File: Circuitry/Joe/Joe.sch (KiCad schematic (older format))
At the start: 41 parts

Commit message: fixed up joe
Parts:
- removed Q? (x4): 2N7000, Package_TO_SOT_THT:TO-92_Inline, symbol Transistor_FET:2N7000
- removed R? (x8): 10k, symbol Device:R
- added BT?: Battery_Cell, symbol Device:Battery_Cell
- added J?: USB_B_Micro, symbol Connector:USB_B_Micro
- added U?: AP2127N-3.3, Package_TO_SOT_SMD:SOT-23, symbol Regulator_Linear:AP2127N-3.3
- R? (x4): value R -> 1k
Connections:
- net labels added: CRYSTAL, D+, D-, RCLK, SER, SRCLK, VBUS, ~SRCLR
- net labels removed: CRY, CRYSTAL2, DATA, E0, E1, E2, MOSO, SCL2, SDA2, SQW2, S_CLR
- wire segments 125 -> 101
- no-connect marks 4 -> 15
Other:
- note removed: "Level Shifters"

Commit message: Joe: RTC changed to soic8, added labels to screw terminal, removed shift regs Burt: added shift reg
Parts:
- removed U?: DS3231M, Package_SO:SOIC-16W_7.5x10.3mm_P1.27mm, symbol Timer_RTC:DS3231M
- removed U?: 74HC595, symbol 74xx:74HC595
- added U?: DS3231MZ, Package_SO:SOIC-8_3.9x4.9mm_P1.27mm, symbol Timer_RTC:DS3231MZ
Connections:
- net labels removed: BL1, BL2, BL3, BL4, BL5, BL6, BL7, BL8, BWL
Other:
- note added: "Burn Wire Output 1 for Pyrolysis"
- note added: "Burn Wire Output 2 for Pyrolysis"
- note added: "Img Sensor Data Input"
- note added: "RX Output for Img Processor"
- note added: "TX Output for Img Processor"
- note added: "Temp Sensor Data Input"
- note removed: "Shift Register (for launcher bw)"
- moved on the sheet: U?
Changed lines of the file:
@@
 	2450 1450 2975 1450
-$Comp
-L Timer_RTC:DS3231M U?
-U 1 1 5D1CA19F
-P 1950 1650
-F 0 "U?" H 1150 2575 50  0000 C CNN
-F 1 "DS3231M" H 900 2575 50  0000 C CNN
-F 2 "Package_SO:SOIC-16W_7.5x10.3mm_P1.27mm" H 1950 1050 50  0001 C CNN
-F 3 "http://datasheets.maximintegrated.com/en/ds/DS3231.pdf" H 2220 1700 50  0001 C CNN
-	1    1950 1650
-	1    0    0    -1
-$EndComp
 $Comp
 L Device:R R?
@@
 Text Label 10875 3150 0    50   ~ 0
 PHO4
-Text Label 6850 4600 2    50   ~ 0
+Text Label 4550 2875 2    50   ~ 0
 TEMP
 Wire Wire Line
@@
 Wire Wire Line
 	10650 2450 10850 2450
-Text Label 6850 4700 2    50   ~ 0
+Text Label 4550 2975 2    50   ~ 0
 CVBS
-$Comp
-L Joe-rescue:UFDFPN8-MC-Custom U?
-U 1 1 5D2D63AB
-P 4925 6900
-F 0 "U?" H 4950 7265 50  0000 C CNN
-F 1 "UFDFPN8-MC" H 4950 7174 50  0000 C CNN
-F 2 "" H 4925 6900 50  0001 C CNN
-F 3 "https://www.st.com/content/ccc/resource/technical/document/datasheet/80/4e/8c/54/f2/63/4c/4a/CD00001012.pdf/files/CD00001012.pdf/jcr:content/translations/en.CD00001012.pdf" H 4925 6900 50  0001 C CNN
-	1    4925 6900
-	1    0    0    -1
-$EndComp
-Wire Wire Line
-	5275 6800 5475 6800
-Text Label 5275 6900 0    50   ~ 0
+Wire Wire Line
+	3725 6025 3925 6025
+Text Label 3725 6125 0    50   ~ 0
 WC
-Text Label 5275 7000 0    50   ~ 0
+Text Label 3725 6225 0    50   ~ 0
 SCL
-Text Label 5275 7100 0    50   ~ 0
+Text Label 3725 6325 0    50   ~ 0
 SDA
 $Comp
 L power:GND #PWR?
 U 1 1 5D2C2E70
-P 4450 7100
-F 0 "#PWR?" H 4450 6850 50  0001 C CNN
-F 1 "GND" H 4455 6927 50  0000 C CNN
-F 2 "" H 4450 7100 50  0001 C CNN
-F 3 "" H 4450 7100 50  0001 C CNN
-	1    4450 7100
-	1    0    0    -1
-$EndComp
-Wire Wire Line
-	4625 7100 4450 7100
+P 2900 6325
+F 0 "#PWR?" H 2900 6075 50  0001 C CNN
+F 1 "GND" H 2905 6152 50  0000 C CNN
+F 2 "" H 2900 6325 50  0001 C CNN
+F 3 "" H 2900 6325 50  0001 C CNN
+	1    2900 6325
+	1    0    0    -1
+$EndComp
+Wire Wire Line
+	3075 6325 2900 6325
 Text Label 10875 4250 0    50   ~ 0
 WC
@@
 Wire Notes Line
 	2650 3825 2650 2475
-Text Notes 4325 6350 0    50   ~ 0
-EEPROM\n
-$Comp
-L 74xx:74HC595 U?
-U 1 1 5D4B08F4
-P 3525 6575
-F 0 "U?" H 2750 7550 50  0000 C CNN
-F 1 "74HC595" H 2875 7450 50  0000 C CNN
-F 2 "" H 3525 6575 50  0001 C CNN
-F 3 "http://www.ti.com/lit/ds/symlink/sn74hc595.pdf" H 3525 6575 50  0001 C CNN
-	1    3525 6575
-	1    0    0    -1
-$EndComp
-Text Notes 6775 4425 0    50   ~ 0
+Text Notes 4475 2700 0    50   ~ 0
 Joe <--> Burt\n
-$Comp
-L power:GND #PWR?
-U 1 1 5D4CD56F
-P 3525 7275
-F 0 "#PWR?" H 3525 7025 50  0001 C CNN
-F 1 "GND" H 3530 7102 50  0000 C CNN
-F 2 "" H 3525 7275 50  0001 C CNN
-F 3 "" H 3525 7275 50  0001 C CNN
-	1    3525 7275
-	1    0    0    -1
-$EndComp
 Text Label 10875 4350 0    50   ~ 0
 SER
-Text Label 3125 6175 2    50   ~ 0
-SER
-Text Label 3925 6175 0    50   ~ 0
-BL1
-Text Label 3925 6275 0    50   ~ 0
-BL2
-Text Label 3925 6375 0    50   ~ 0
-BL3
-Text Label 3925 6475 0    50   ~ 0
-BL4
-Text Label 3925 6575 0    50   ~ 0
-BL5
-Text Label 3925 6675 0    50   ~ 0
-BL6
-Text Label 3925 6775 0    50   ~ 0
-BL7
-Text Label 3925 6875 0    50   ~ 0
-BL8
-Text Label 3125 6775 2    50   ~ 0
-OE
 Text Label 10875 4450 0    50   ~ 0
 OE
@@
 Text Label 10850 2150 0    50   ~ 0
 BP2
-Text Label 3125 6475 2    50   ~ 0
-~SRCLR
 Wire Notes Line
 	2650 3875 4150 3875
@@
 Wire Notes Line
 	2650 3875 2650 5375
-Wire Notes Line
-	2650 5425 4150 5425
-Wire Notes Line
-	4150 5425 4150 7750
-Wire Notes Line
-	4150 7750 2650 7750
-Wire Notes Line
-	2650 7750 2650 5425
-Text Notes 2700 5550 0    50   ~ 0
-Shift Register (for launcher bw)
 $Comp
 L Joe-rescue:DF12-20DS-Custom U?
@@
 Wire Notes Line
 	6200 500  4050 500
-Text Label 6850 5200 2    50   ~ 0
-BWL
-Text Label 6850 5000 2    50   ~ 0
+Text Label 4550 3275 2    50   ~ 0
 BP1
-Text Label 6850 5100 2    50   ~ 0
+Text Label 4550 3375 2    50   ~ 0
 BP2
 $Comp
@@
 Wire Wire Line
 	10650 2550 10875 2550
-Text Label 3125 6375 2    50   ~ 0
-SRCLK
-Text Label 3125 6675 2    50   ~ 0
-RCLK
-Wire Wire Line
-	4625 7000 4450 7000
-Wire Wire Line
-	4450 7000 4450 7100
-Connection ~ 4450 7100
-Wire Wire Line
-	4625 6900 4450 6900
-Wire Wire Line
-	4450 6900 4450 7000
-Connection ~ 4450 7000
-Wire Wire Line
-	4625 6800 4450 6800
-Wire Wire Line
-	4450 6800 4450 6900
-Connection ~ 4450 6900
+Wire Wire Line
+	3075 6225 2900 6225
+Wire Wire Line
+	2900 6225 2900 6325
+Connection ~ 2900 6325
+Wire Wire Line
+	3075 6125 2900 6125
+Wire Wire Line
+	2900 6125 2900 6225
+Connection ~ 2900 6225
+Wire Wire Line
+	3075 6025 2900 6025
+Wire Wire Line
+	2900 6025 2900 6125
+Connection ~ 2900 6125
 $Comp
 L power:+3V3 #PWR?
 U 1 1 5D3707C8
-P 5475 6800
-F 0 "#PWR?" H 5475 6650 50  0001 C CNN
-F 1 "+3V3" H 5490 6973 50  0000 C CNN
-F 2 "" H 5475 6800 50  0001 C CNN
-F 3 "" H 5475 6800 50  0001 C CNN
-	1    5475 6800
-	1    0    0    -1
-$EndComp
-$Comp
-L power:+3V3 #PWR?
-U 1 1 5D371FC8
-P 3525 5975
-F 0 "#PWR?" H 3525 5825 50  0001 C CNN
-F 1 "+3V3" H 3540 6148 50  0000 C CNN
-F 2 "" H 3525 5975 50  0001 C CNN
-F 3 "" H 3525 5975 50  0001 C CNN
-	1    3525 5975
+P 3925 6025
+F 0 "#PWR?" H 3925 5875 50  0001 C CNN
+F 1 "+3V3" H 3940 6198 50  0000 C CNN
+F 2 "" H 3925 6025 50  0001 C CNN
+F 3 "" H 3925 6025 50  0001 C CNN
+	1    3925 6025
 	1    0    0    -1
 $EndComp
@@
 Text Label 10875 3950 0    50   ~ 0
 ~SRCLR
+Text Notes 2775 5575 0    50   ~ 0
+EEPROM\n
+$Comp
+L Joe-rescue:UFDFPN8-MC-Custom U?
+U 1 1 5D2D63AB
+P 3375 6125
+F 0 "U?" H 3400 6490 50  0000 C CNN
+F 1 "UFDFPN8-MC" H 3400 6399 50  0000 C CNN
+F 2 "" H 3375 6125 50  0001 C CNN
+F 3 "https://www.st.com/content/ccc/resource/technical/document/datasheet/80/4e/8c/54/f2/63/4c/4a/CD00001012.pdf/files/CD00001012.pdf/jcr:content/translations/en.CD00001012.pdf" H 3375 6125 50  0001 C CNN
+	1    3375 6125
+	1    0    0    -1
+$EndComp
+Text Label 4550 3075 2    50   ~ 0
+TX
+Text Label 4550 3175 2    50   ~ 0
+RX
+Text Label 4550 3475 2    50   ~ 0
+SER
+Text Label 4550 3575 2    50   ~ 0
+SRCLK
+Text Label 4550 3675 2    50   ~ 0
+RCLK
+$Comp
+L Timer_RTC:DS3231MZ U?
+U 1 1 5D2C648B
+P 1950 1650
+F 0 "U?" H 1950 1161 50  0000 C CNN
+F 1 "DS3231MZ" H 1950 1070 50  0000 C CNN
+F 2 "Package_SO:SOIC-8_3.9x4.9mm_P1.27mm" H 1950 1150 50  0001 C CNN
+F 3 "http://datasheets.maximintegrated.com/en/ds/DS3231M.pdf" H 1950 1050 50  0001 C CNN
+	1    1950 1650
+	1    0    0    -1
+$EndComp
+Text Notes 5325 2875 0    39   ~ 0
+Temp Sensor Data Input
+Text Notes 5325 2975 0    39   ~ 0
+Img Sensor Data Input
+Text Notes 5325 3075 0    39   ~ 0
+TX Output for Img Processor
+Text Notes 5325 3175 0    39   ~ 0
+RX Output for Img Processor
+Text Notes 5325 3275 0    39   ~ 0
+Burn Wire Output 1 for Pyrolysis
+Text Notes 5325 3375 0    39   ~ 0
+Burn Wire Output 2 for Pyrolysis
 $EndSCHEMATC

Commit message: complete screw terminal, labeling, etc. done for FINAL REVIEW
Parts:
- added J?: Screw_Terminal_01x09, symbol Connector:Screw_Terminal_01x09
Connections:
- net OE is gone; now on net PLED2: U?.36 (PF7)
- net BP1: now also J?.5 (Pin_5)
- net BP2: now also J?.6 (Pin_6)
- net CVBS: now also J?.2 (Pin_2)
- net RCLK: now also J?.9 (Pin_9)
- net RX: now also J?.4 (Pin_4)
- net SER: now also J?.7 (Pin_7)
- net SRCLK: now also J?.8 (Pin_8)
- net TEMP: now also J?.1 (Pin_1)
- net TX: now also J?.3 (Pin_3)
- net PLED2: now reaches U?.33 (~HWB~/PE2)
- net PLED2: now also D?.2 (A)
- net PLED1: now reaches U?.8 (PB0)
- net PLED1: now also D?.2 (A)
- net PLED3: now reaches D?.2 (A)
- net ~SRCLR: no longer names the net of U?.41 (PF0)
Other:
- note added: "5V to 3.3V Regulator\n"
- note added: "Data Storage: USB and SD"
- note added: "Input = Data from Burt to Joe\nOutput = Data from Joe to Burt"
- note added: "Reg Clk Output for Shift Regs\n"
- note added: "Serial Clk Output for Shift Regs\n"
- note added: "Serial Output for Shift Regs"
- note removed: "Joe <--> Burt\n"
- moved on the sheet: C?, D?, J?, R?, U?

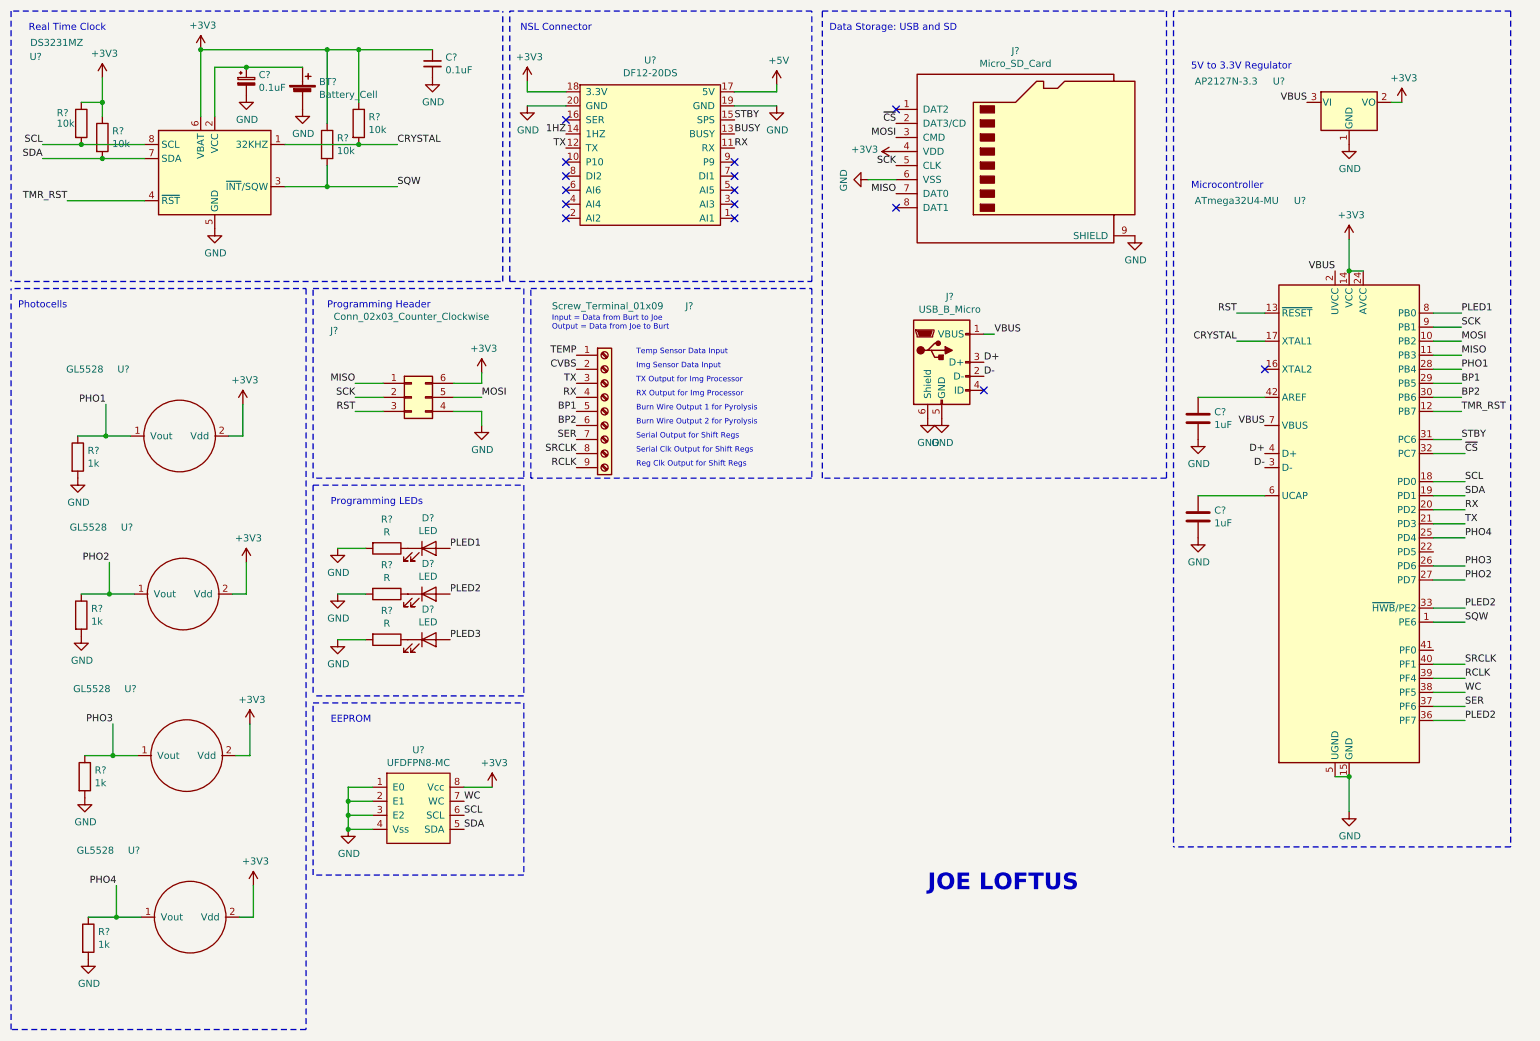
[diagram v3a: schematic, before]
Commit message: part URLs for Joe Loftus
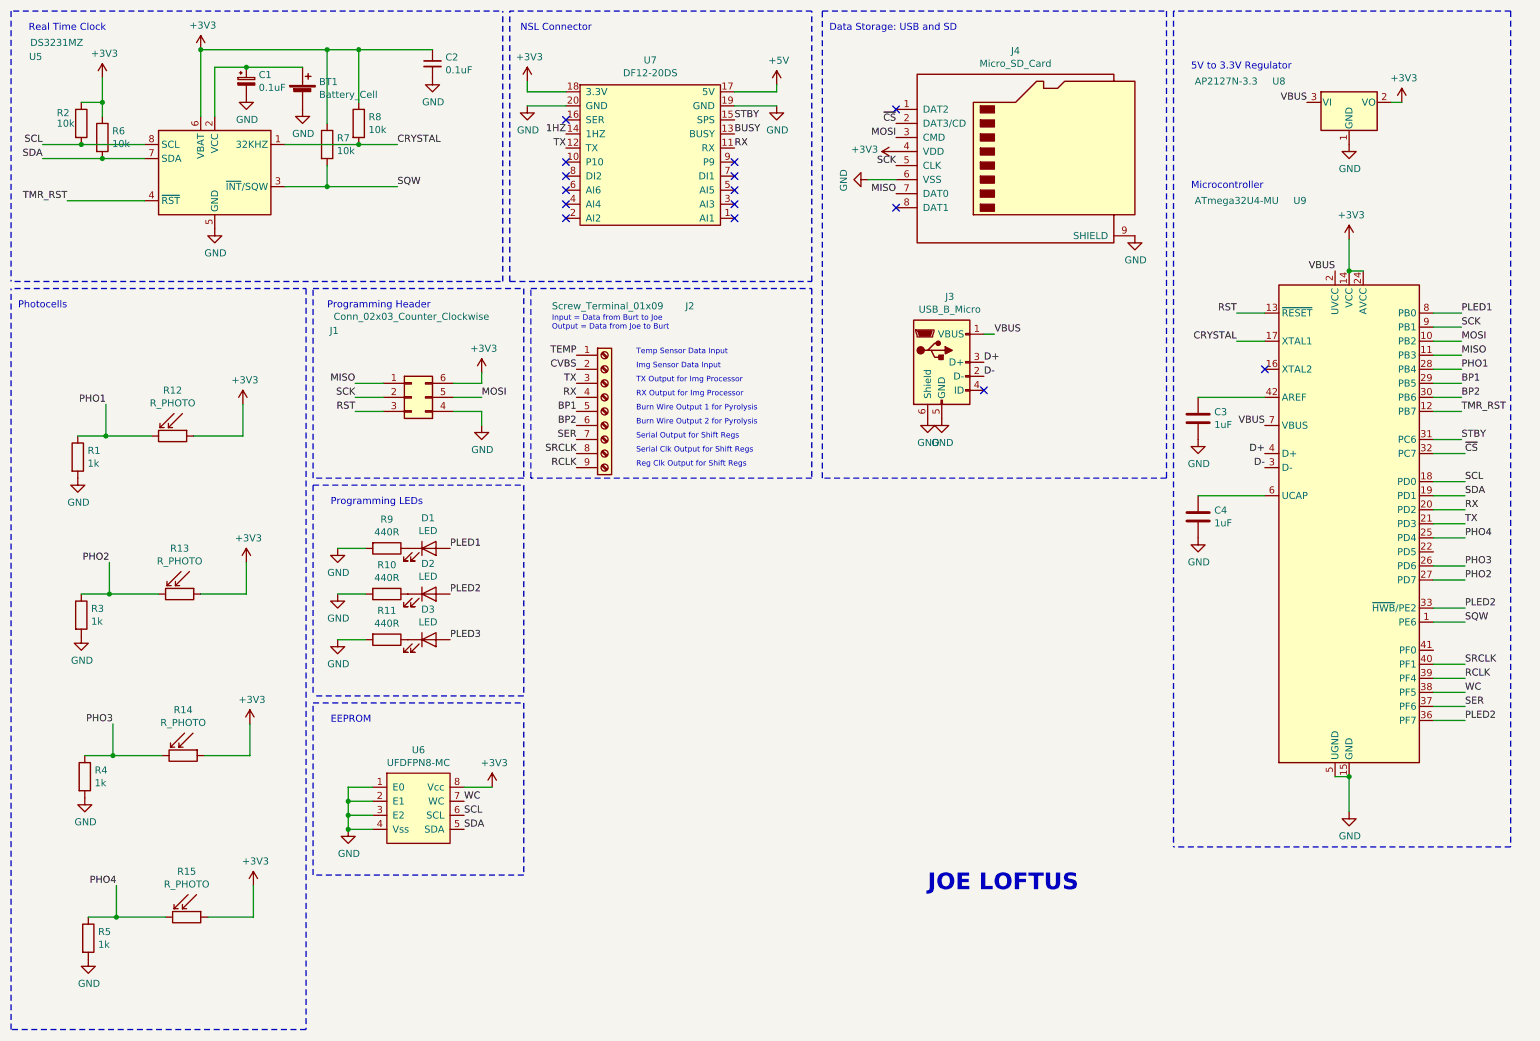
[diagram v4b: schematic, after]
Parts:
- removed U? (x4): GL5528, symbol Joe-rescue:GL5528-Custom
- added R12, R13, R14, R15: R_PHOTO, symbol Device:R_PHOTO
- BT1: renamed from BT?; Part URL (none) -> https://www.digikey.com/product-detail/en/keystone-electron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
- C1, C2: renamed from C?; Part URL (none) -> https://www.digikey.com/product-detail/en/knowles-syfer/060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
- C3, C4: renamed from C?; Part URL (none) -> https://www.digikey.com/product-detail/en/murata-electronic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
- D1, D2, D3: renamed from D?; Part URL (none) -> https://www.digikey.com/product-detail/en/lite-on-inc/LTST-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
- J1: renamed from J?; Part URL (none) -> https://www.digikey.com/product-detail/en/sullins-connector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
- J2: renamed from J?; Part URL (none) -> https://www.digikey.com/product-detail/en/amphenol-anytek/V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
- J3: renamed from J?; Part URL (none) -> https://www.digikey.com/product-detail/en/amphenol-icc-fci/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
- J4: renamed from J?; Part URL (none) -> https://www.digikey.com/product-detail/en/molex/1051620001/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
- R1, R3, R4, R5: renamed from R?; Part URL (none) -> https://www.digikey.com/product-detail/en/panasonic-electro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
- R10, R11, R9: renamed from R?; value R -> 440R; Part URL (none) -> https://www.digikey.com/product-detail/en/vishay-foil-resis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
- R2, R6, R7, R8: renamed from R?; Part URL (none) -> https://www.digikey.com/product-detail/en/te-connectivity-p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
- U5: renamed from U?; Part URL (none) -> https://www.digikey.com/product-detail/en/maxim-integrated/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
- U6: renamed from U?; Part URL (none) -> https://www.digikey.com/products/en/integrated-circuits-ics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
- U7: renamed from U?; Part URL (none) -> https://www.digikey.com/product-detail/en/hirose-electric-c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
- U8: renamed from U?; Part URL (none) -> https://www.digikey.com/product-detail/en/diodes-incorporat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
- U9: renamed from U?; Part URL (none) -> https://www.digikey.com/product-detail/en/microchip-technol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
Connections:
- net +3V3: now also R12.1, R13.1, R14.1, R15.1
- net PHO1: now also R12.2
- net PHO2: now also R13.2
- net PHO3: now also R14.2
- net PHO4: now also R15.2

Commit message: joe done for final review
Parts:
- R1, R3, R4, R5: Part URL https://www.digikey.com/product-detail/en/panasonic-electro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 -> https://www.digikey.com/product-detail/en/yageo/RT0603DRD07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
- R10, R11, R9: Part URL https://www.digikey.com/product-detail/en/vishay-foil-resis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 -> https://www.digikey.com/product-detail/en/yageo/RC0603FR-07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
- R2, R6, R7, R8: Part URL https://www.digikey.com/product-detail/en/te-connectivity-p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 -> https://www.digikey.com/product-detail/en/yageo/RT0603BRD07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
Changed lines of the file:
@@
 F 2 "" V 3105 4325 50  0001 C CNN
 F 3 "~" H 3175 4325 50  0001 C CNN
-F 4 "https://www.digikey.com/product-detail/en/vishay-foil-resistors-division-of-vishay-precision-group/Y1625440R000Q24W/Y1625440R000Q24W-ND/6029380" H 3175 4325 50  0001 C CNN "Part URL"
+F 4 "https://www.digikey.com/product-detail/en/yageo/RC0603FR-07442RL/311-442HRCT-ND/730189" H 3175 4325 50  0001 C CNN "Part URL"
 	1    3175 4325
 	0    1    1    0
@@
 F 2 "" V 3105 4650 50  0001 C CNN
 F 3 "~" H 3175 4650 50  0001 C CNN
-F 4 "https://www.digikey.com/product-detail/en/vishay-foil-resistors-division-of-vishay-precision-group/Y1625440R000Q24W/Y1625440R000Q24W-ND/6029380" H 3175 4650 50  0001 C CNN "Part URL"
+F 4 "https://www.digikey.com/product-detail/en/yageo/RC0603FR-07442RL/311-442HRCT-ND/730189" H 3175 4650 50  0001 C CNN "Part URL"
 	1    3175 4650
 	0    1    1    0
@@
 F 2 "" V 3105 4975 50  0001 C CNN
 F 3 "~" H 3175 4975 50  0001 C CNN
-F 4 "https://www.digikey.com/product-detail/en/vishay-foil-resistors-division-of-vishay-precision-group/Y1625440R000Q24W/Y1625440R000Q24W-ND/6029380" H 3175 4975 50  0001 C CNN "Part URL"
+F 4 "https://www.digikey.com/product-detail/en/yageo/RC0603FR-07442RL/311-442HRCT-ND/730189" H 3175 4975 50  0001 C CNN "Part URL"
 	1    3175 4975
 	0    1    1    0
@@
 F 2 "" V 1080 1400 50  0001 C CNN
 F 3 "~" H 1150 1400 50  0001 C CNN
-F 4 "https://www.digikey.com/product-detail/en/te-connectivity-passive-product/CRGCQ2010F10K/A129944CT-ND/8577776" H 1150 1400 50  0001 C CNN "Part URL"
+F 4 "https://www.digikey.com/product-detail/en/yageo/RT0603BRD0710KL/YAG1236CT-ND/4340589" H 1150 1400 50  0001 C CNN "Part URL"
 	1    1150 1400
 	1    0    0    -1
@@
 F 2 "" V 930 1300 50  0001 C CNN
 F 3 "~" H 1000 1300 50  0001 C CNN
-F 4 "https://www.digikey.com/product-detail/en/te-connectivity-passive-product/CRGCQ2010F10K/A129944CT-ND/8577776" H 1000 1300 50  0001 C CNN "Part URL"
+F 4 "https://www.digikey.com/product-detail/en/yageo/RT0603BRD0710KL/YAG1236CT-ND/4340589" H 1000 1300 50  0001 C CNN "Part URL"
 	1    1000 1300
 	1    0    0    -1
@@
 F 2 "" V 2680 1450 50  0001 C CNN
 F 3 "~" H 2750 1450 50  0001 C CNN
-F 4 "https://www.digikey.com/product-detail/en/te-connectivity-passive-product/CRGCQ2010F10K/A129944CT-ND/8577776" H 2750 1450 50  0001 C CNN "Part URL"
+F 4 "https://www.digikey.com/product-detail/en/yageo/RT0603BRD0710KL/YAG1236CT-ND/4340589" H 2750 1450 50  0001 C CNN "Part URL"
 	1    2750 1450
 	1    0    0    -1
@@
 F 2 "" V 2905 1300 50  0001 C CNN
 F 3 "~" H 2975 1300 50  0001 C CNN
-F 4 "https://www.digikey.com/product-detail/en/te-connectivity-passive-product/CRGCQ2010F10K/A129944CT-ND/8577776" H 2975 1300 50  0001 C CNN "Part URL"
+F 4 "https://www.digikey.com/product-detail/en/yageo/RT0603BRD0710KL/YAG1236CT-ND/4340589" H 2975 1300 50  0001 C CNN "Part URL"
 	1    2975 1300
 	1    0    0    -1
@@
 F 2 "" V 905 3675 50  0001 C CNN
 F 3 "~" H 975 3675 50  0001 C CNN
-F 4 "https://www.digikey.com/product-detail/en/panasonic-electronic-components/ERJ-6GEYJ102V/P1.0KACT-ND/42833" H 975 3675 50  0001 C CNN "Part URL"
+F 4 "https://www.digikey.com/product-detail/en/yageo/RT0603DRD071KL/311-1.0KDCT-ND/1035738" H 975 3675 50  0001 C CNN "Part URL"
 	1    975  3675
 	1    0    0    -1
@@
 F 2 "" V 930 4800 50  0001 C CNN
 F 3 "~" H 1000 4800 50  0001 C CNN
-F 4 "https://www.digikey.com/product-detail/en/panasonic-electronic-components/ERJ-6GEYJ102V/P1.0KACT-ND/42833" H 1000 4800 50  0001 C CNN "Part URL"
+F 4 "https://www.digikey.com/product-detail/en/yageo/RT0603DRD071KL/311-1.0KDCT-ND/1035738" H 1000 4800 50  0001 C CNN "Part URL"
 	1    1000 4800
 	1    0    0    -1
@@
 F 2 "" V 955 5950 50  0001 C CNN
 F 3 "~" H 1025 5950 50  0001 C CNN
-F 4 "https://www.digikey.com/product-detail/en/panasonic-electronic-components/ERJ-6GEYJ102V/P1.0KACT-ND/42833" H 1025 5950 50  0001 C CNN "Part URL"
+F 4 "https://www.digikey.com/product-detail/en/yageo/RT0603DRD071KL/311-1.0KDCT-ND/1035738" H 1025 5950 50  0001 C CNN "Part URL"
 	1    1025 5950
 	1    0    0    -1
@@
 F 2 "" V 980 7100 50  0001 C CNN
 F 3 "~" H 1050 7100 50  0001 C CNN
-F 4 "https://www.digikey.com/product-detail/en/panasonic-electronic-components/ERJ-6GEYJ102V/P1.0KACT-ND/42833" H 1050 7100 50  0001 C CNN "Part URL"
+F 4 "https://www.digikey.com/product-detail/en/yageo/RT0603DRD071KL/311-1.0KDCT-ND/1035738" H 1050 7100 50  0001 C CNN "Part URL"
 	1    1050 7100
 	1    0    0    -1
